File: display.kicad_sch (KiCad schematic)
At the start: 8 parts, among them U1 MAX7221xWG, U3 CC56-12GWA, U4 CC56-12GWA

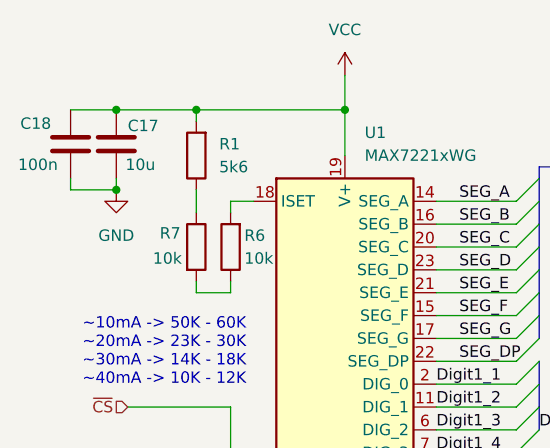
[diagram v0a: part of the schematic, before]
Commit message: Decoupling capacitor change from 10u to 1u
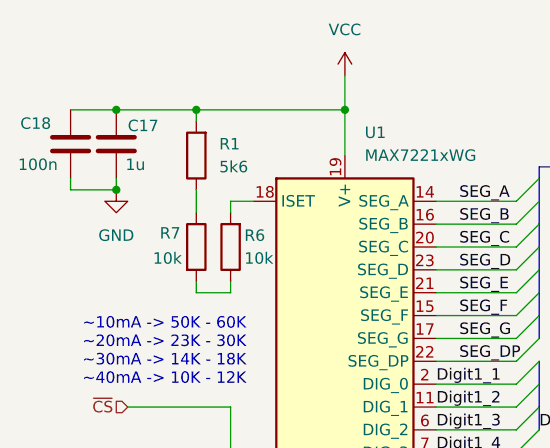
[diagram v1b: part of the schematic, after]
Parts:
- C17: value 10u -> 1u
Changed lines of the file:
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@@
 			)
 		)
-		(property "Value" "10u"
+		(property "Value" "1u"
 			(at 69.596 69.596 0)
 			(effects

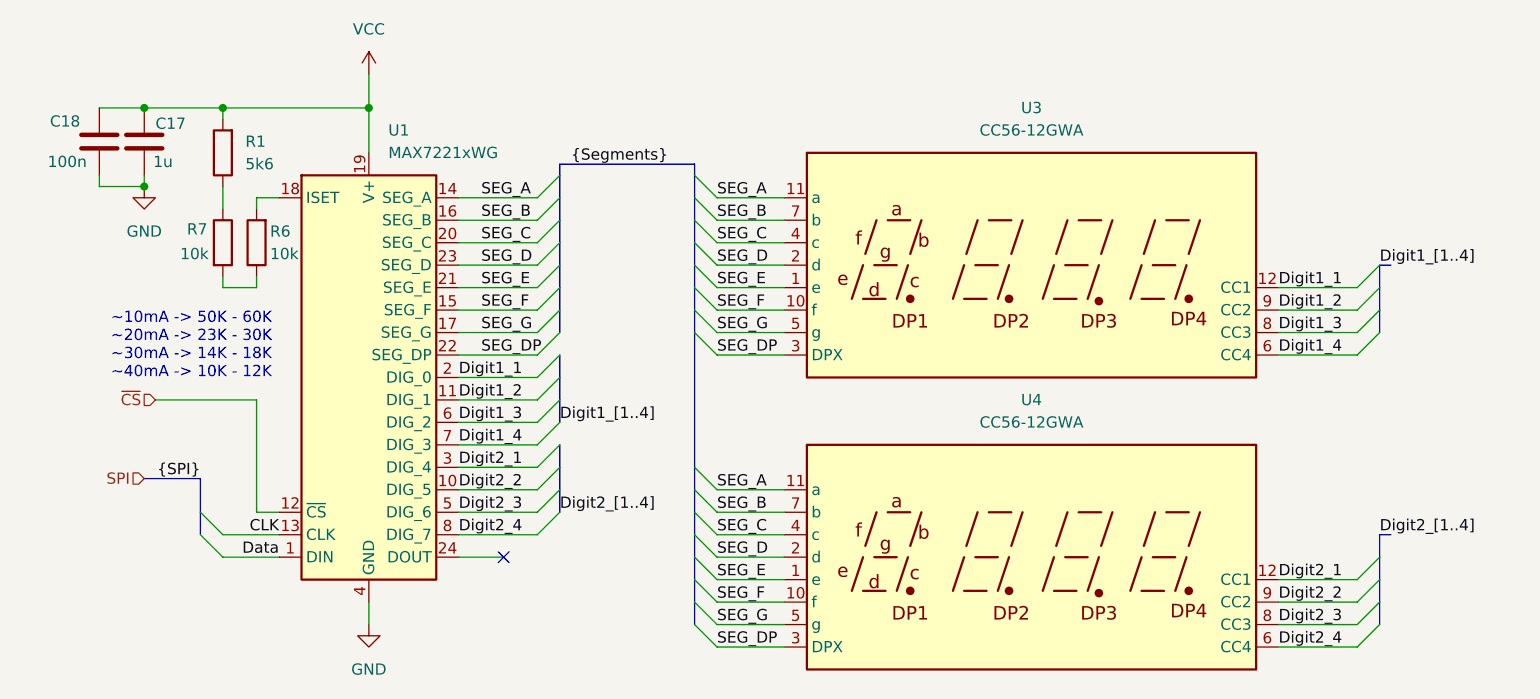
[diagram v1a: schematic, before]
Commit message: Resolve ERC warnings
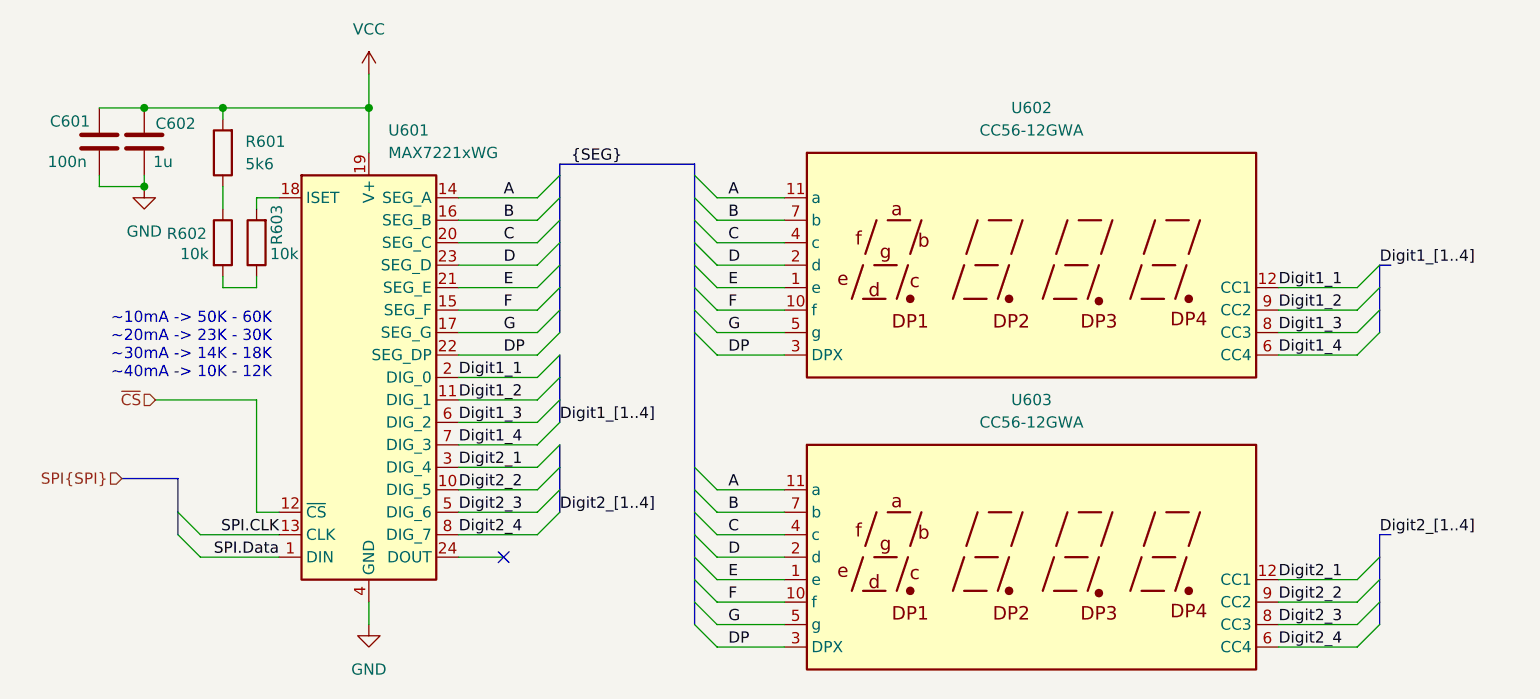
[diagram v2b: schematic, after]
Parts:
- renumbered C18 to C601, C17 to C602, R1 to R601, R7 to R602, R6 to R603, U1 to U601, U3 to U602, U4 to U603
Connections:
- net CLK renamed SPI.CLK
- net Data renamed SPI.Data
- net SEG_A renamed A
- net SEG_B renamed B
- net SEG_C renamed C
- net SEG_D renamed D
- net SEG_DP renamed DP
- net SEG_E renamed E
- net SEG_F renamed F
- net SEG_G renamed G

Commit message: Add Testpoints
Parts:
- added TP14: ~{CS}, symbol Connector:TestPoint
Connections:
- net ~{CS}: now also TP14.1
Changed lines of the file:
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@@
+	)
+	(junction
+		(at 72.39 96.52)
+		(diameter 0)
+		(color 0 0 0 0)
 	)
 	(junction
@@
 		)
 	)
+	(wire
+		(pts
+			(xy 72.39 96.52) (xy 81.28 96.52)
+		)
+		(stroke
+			(width 0)
+			(type default)
+		)
+	)
 	(bus
 		(pts
@@
 	(wire
 		(pts
-			(xy 69.85 96.52) (xy 81.28 96.52)
+			(xy 69.85 96.52) (xy 72.39 96.52)
 		)
 		(stroke
@@
 					(unit 1)
 				)
+			)
+		)
+	)
+	(symbol
+		(lib_id "Connector:TestPoint")
+		(at 72.39 96.52 180)
+		(unit 1)
+		(exclude_from_sim no)
+		(in_bom yes)
+		(on_board yes)
+		(dnp no)
+		(fields_autoplaced yes)
+		(property "Reference" "TP14"
+			(at 74.93 98.5519 0)
+			(effects
+				(font
+					(size 1.27 1.27)
+				)
+				(justify right)
+			)
+		)
+		(property "Value" "~{CS}"
+			(at 74.93 101.0919 0)
+			(effects
+				(font
+					(size 1.27 1.27)
+				)
+				(justify right)
+			)
+		)
+		(property "Footprint" ""
+			(at 67.31 96.52 0)
+			(effects
+				(font
+					(size 1.27 1.27)
+				)
+				(hide yes)
+			)
+		)
+		(property "Datasheet" "~"
+			(at 67.31 96.52 0)
+			(effects
+				(font
+					(size 1.27 1.27)
+				)
+				(hide yes)
+			)
+		)
+		(property "Description" "test point"
+			(at 72.39 96.52 0)
+			(effects
+				(font
+					(size 1.27 1.27)
+				)
+				(hide yes)
+			)
+		)
+		(pin "1"
+		)
+		(instances
+			(project "LifeCounter"
+				(path "/16b3e55a-9d75-49bf-a6fe-25414eb3d7da/672d503e-18e4-4d43-9df6-e02286c9b23c"
+					(reference "TP14")
+					(unit 1)
+				)

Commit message: Footprint selection
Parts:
- C601, C602: footprint Capacitor_SMD:C_0805_2012Metric_Pad1.18x1.45mm_HandSolder -> Capacitor_SMD:C_1206_3216Metric_Pad1.33x1.80mm_HandSolder
- R601, R602, R603: footprint Resistor_SMD:R_0805_2012Metric_Pad1.20x1.40mm_HandSolder -> Resistor_SMD:R_1206_3216Metric_Pad1.30x1.75mm_HandSolder
- TP14: footprint (none) -> TestPoint:TestPoint_Pad_D1.0mm
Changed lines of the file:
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@@
 			)
 		)
-		(property "Footprint" "Resistor_SMD:R_0805_2012Metric_Pad1.20x1.40mm_HandSolder"
+		(property "Footprint" "Resistor_SMD:R_1206_3216Metric_Pad1.30x1.75mm_HandSolder"
 			(at 75.692 78.74 90)
 			(effects
@@
 			)
 		)
-		(property "Footprint" "Resistor_SMD:R_0805_2012Metric_Pad1.20x1.40mm_HandSolder"
+		(property "Footprint" "Resistor_SMD:R_1206_3216Metric_Pad1.30x1.75mm_HandSolder"
 			(at 79.248 68.58 90)
 			(effects
@@
 			)
 		)
-		(property "Footprint" "Capacitor_SMD:C_0805_2012Metric_Pad1.18x1.45mm_HandSolder"
+		(property "Footprint" "Capacitor_SMD:C_1206_3216Metric_Pad1.33x1.80mm_HandSolder"
 			(at 64.4652 71.12 0)
 			(effects
@@
 			)
 		)
-		(property "Footprint" "Capacitor_SMD:C_0805_2012Metric_Pad1.18x1.45mm_HandSolder"
+		(property "Footprint" "Capacitor_SMD:C_1206_3216Metric_Pad1.33x1.80mm_HandSolder"
 			(at 69.5452 71.12 0)
 			(effects
@@
 			)
 		)
-		(property "Footprint" ""
+		(property "Footprint" "TestPoint:TestPoint_Pad_D1.0mm"
 			(at 67.31 96.52 0)
 			(effects
@@
 			)
 		)
-		(property "Footprint" "Resistor_SMD:R_0805_2012Metric_Pad1.20x1.40mm_HandSolder"
+		(property "Footprint" "Resistor_SMD:R_1206_3216Metric_Pad1.30x1.75mm_HandSolder"
 			(at 83.058 78.74 90)
 			(effects
